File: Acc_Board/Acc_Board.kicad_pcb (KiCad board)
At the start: 2 copper layers, 165.1 x 69.8 mm, 58 parts, among them J1 1053091202, J11 1053091202, J12 776087-1, J2 1053091202, J3 1053091202, J4 1053091202, J5 1053091202, J6 1053091202, J7 IsoSPI, J9 1053091202, K1 Relay_SPST-NO, K2 Latching Relay, U1 ISO1050DUB, U10 DK1A1B-12V, U11 LM555N, U12 LTC6820, U13 R-78B5.0-2.0, U2 NUCLEO-L432KC, U4 PQDE6W-Q110-S5-H-D, U5 NAND, U6 NSL-32, U7 DK1A1B-12V, U8 NSL-32, U9 NSL-32

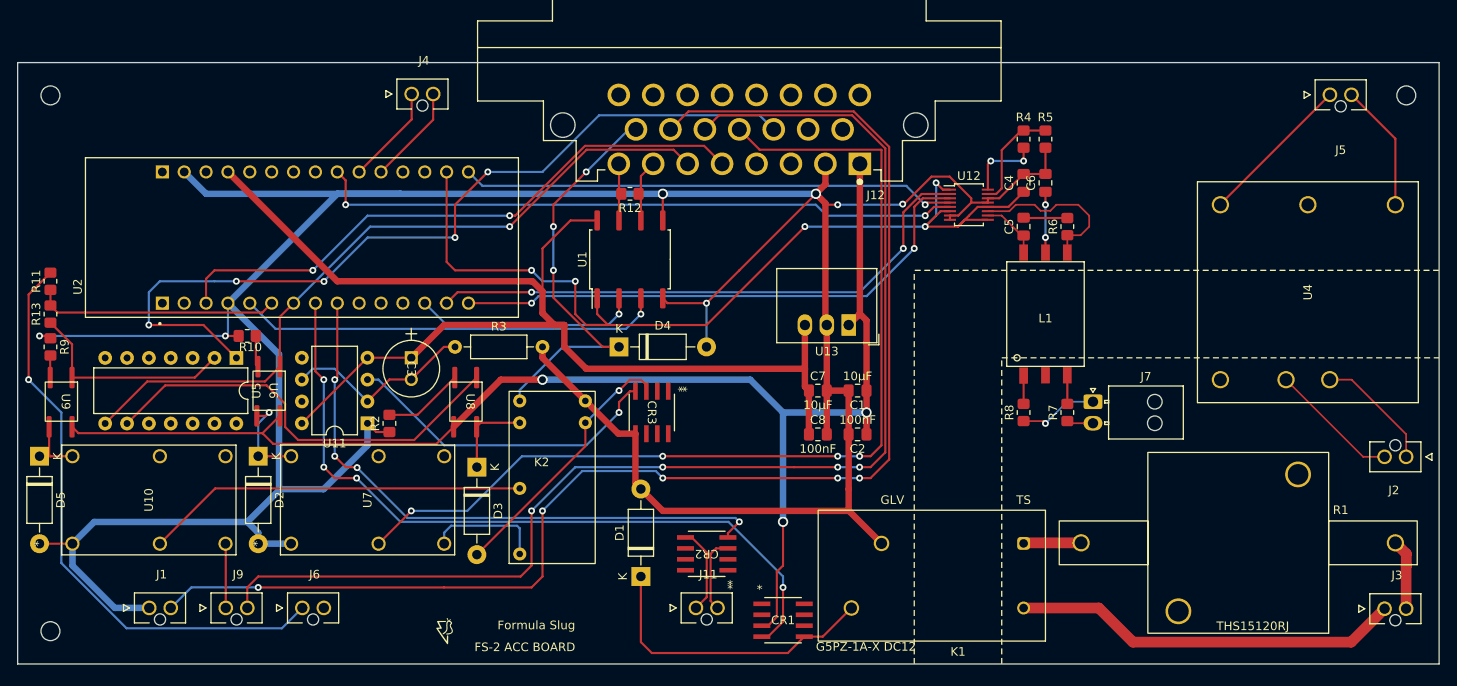
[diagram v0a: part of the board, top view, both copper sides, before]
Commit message: added 3d model for precharge resistor for acc board
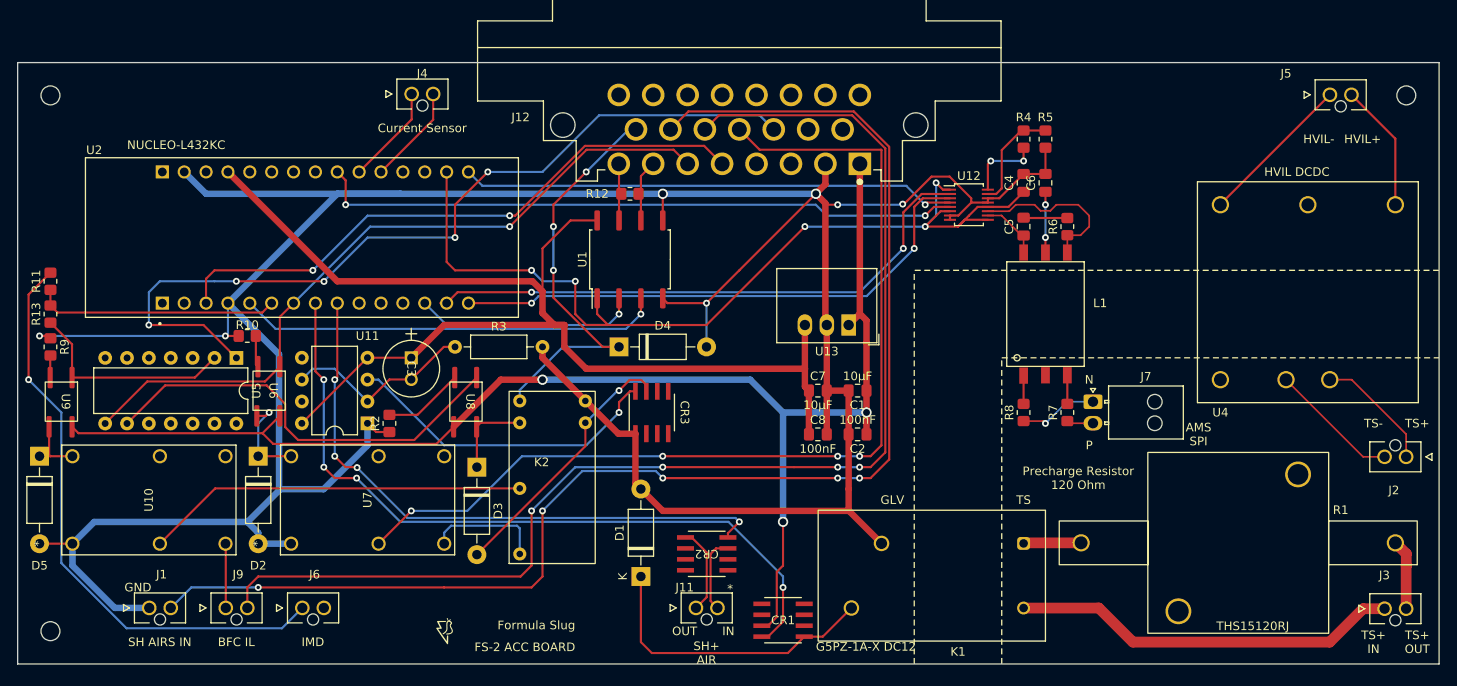
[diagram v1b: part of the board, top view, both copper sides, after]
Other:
- board text added: "AMS SPI"
- board text added: "BFC IL"
- board text added: "Current Sensor"
- board text added: "GND"
- board text added: "HVIL DCDC"
- board text added: "HVIL+"
- board text added: "HVIL-"
- board text added: "IMD"
- board text added: "IN"
- board text added: "N"
- board text added: "NUCLEO-L432KC"
- board text added: "OUT"
- board text added: "P"
- board text added: "Precharge Resistor 120 Ohm"
- board text added: "SH AIRS IN"
- board text added: "SH+ AIR"
- board text added: "TS+"
- board text added: "TS+ IN"
- board text added: "TS+ OUT"
- board text added: "TS-"

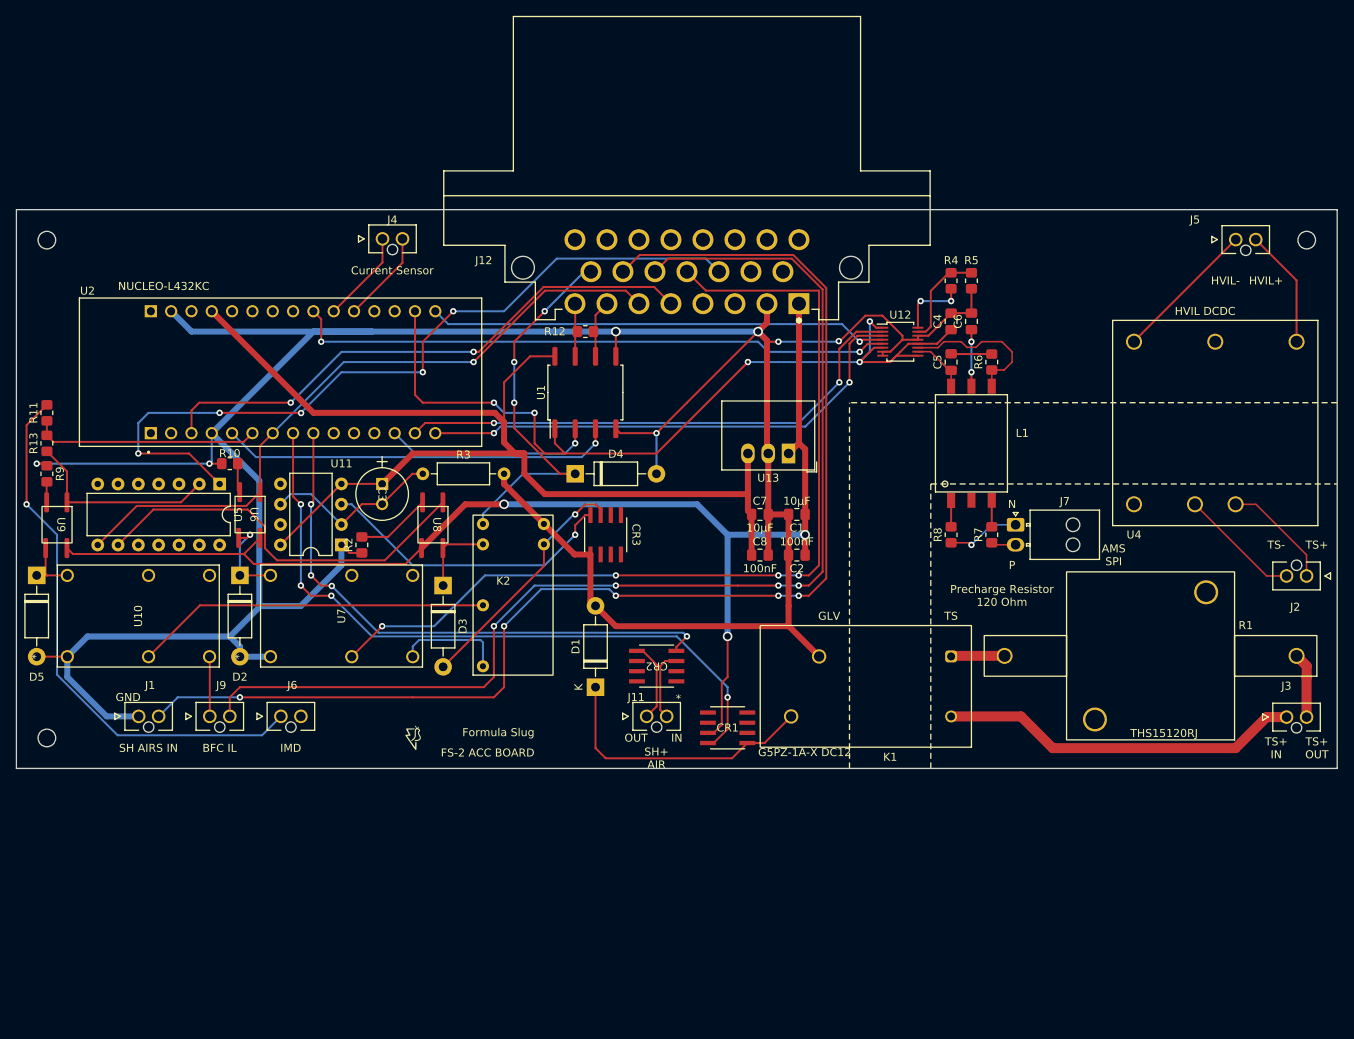
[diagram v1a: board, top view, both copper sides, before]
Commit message: Fixed op amps for current sensor on acc board
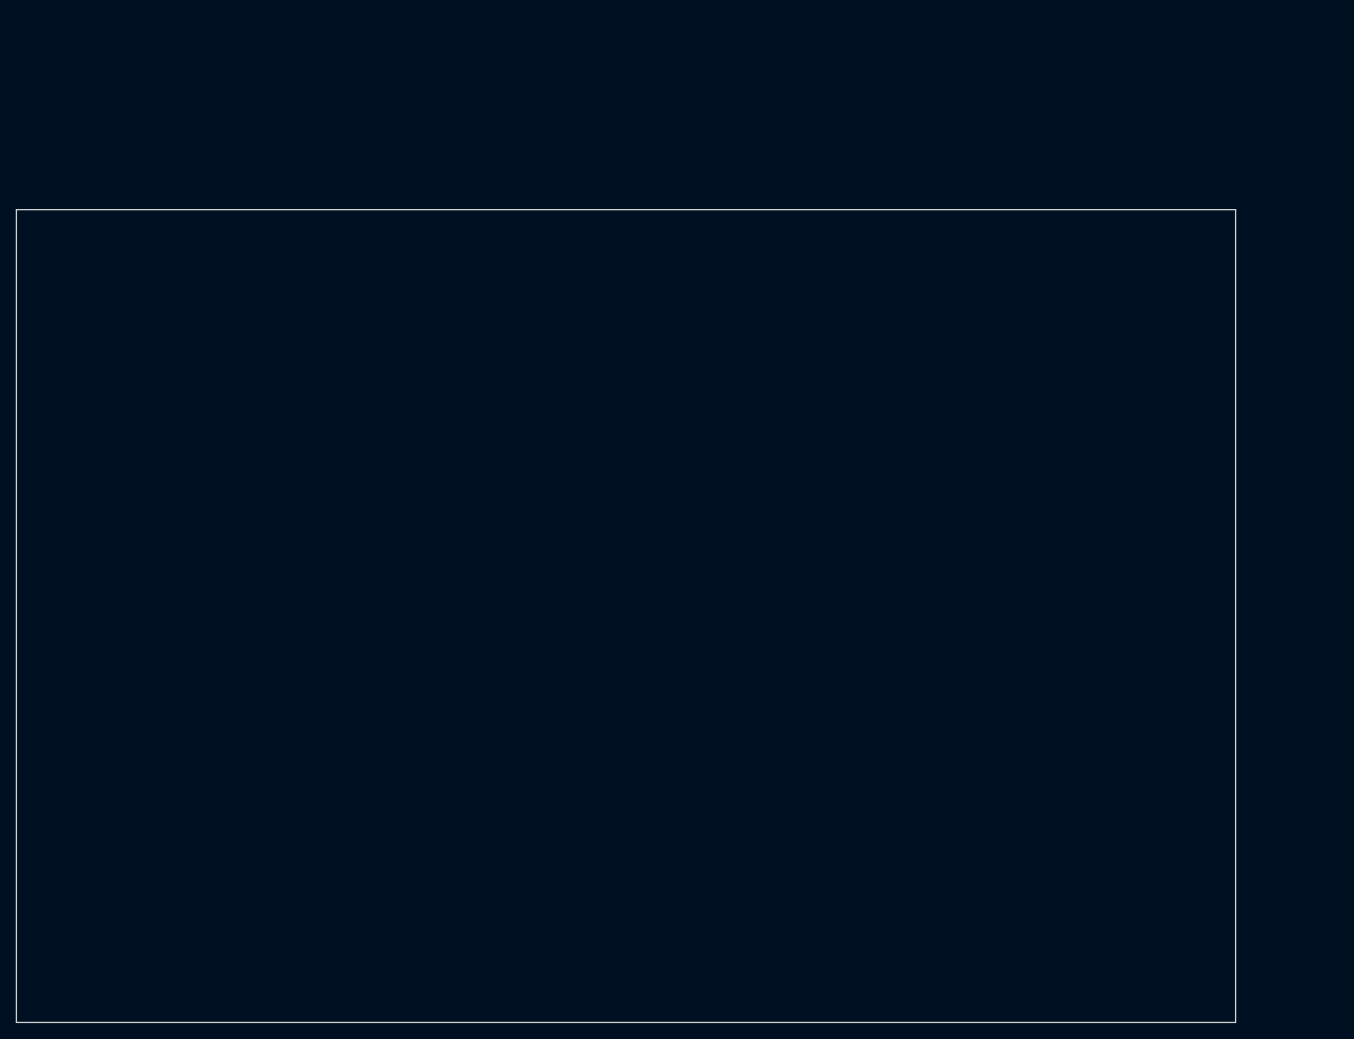
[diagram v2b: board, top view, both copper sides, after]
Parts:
- removed C1, C7: 10µF, Capacitor_SMD:C_0805_2012Metric_Pad1.18x1.45mm_HandSolder
- removed C2, C8: 100nF, Capacitor_SMD:C_0805_2012Metric_Pad1.18x1.45mm_HandSolder
- removed C3: ECA-2DHG010 1uF, 1FS_2_Global_Footprint_Library:PCAP_63x112_PAN
- removed C4, C6: 10nF, Capacitor_SMD:C_0805_2012Metric_Pad1.18x1.45mm_HandSolder
- removed C5: 15pF, Capacitor_SMD:C_0805_2012Metric_Pad1.18x1.45mm_HandSolder
- removed CR1, CR2, CR3: STS6NF20V, 1FS_2_Global_Footprint_Library:SO-8_STM
- removed D1: 1N4001, Diode_THT:D_DO-41_SOD81_P10.16mm_Horizontal
- removed D2, D3, D4, D5: D, Diode_THT:D_DO-41_SOD81_P10.16mm_Horizontal
- removed G***: LOGO, 1FS_2_Global_Footprint_Library:FORMULA SLUG
- removed J1, J11, J2, J3, J4, J5, J6, J9: 1053091202, 1FS_2_Global_Footprint_Library:MOLEX_1053091202
- removed J12: 776087-1, 1FS_2_Global_Footprint_Library:TE_776087-1
- removed J7: IsoSPI, Connector_Molex:Molex_Nano-Fit_105313-xx02_1x02_P2.50mm_Horizontal
- removed K1: Relay_SPST-NO, 1FS_2_Global_Footprint_Library:G5PZ-1A-X DC12
- removed K2: Latching Relay, 1FS_2_Global_Footprint_Library:Omron G6BK-1114P-US
- removed L1: HM2113ZNL, 1FS_2_Global_Footprint_Library:HM2113ZNL
- removed R1: 120, 1FS_2_Global_Footprint_Library:THS15120RJ
- removed R10, R2, R9: 480, Resistor_SMD:R_0805_2012Metric_Pad1.20x1.40mm_HandSolder
- removed R11: 1.6K, Resistor_SMD:R_0805_2012Metric_Pad1.20x1.40mm_HandSolder
- removed R12: 120, Resistor_SMD:R_0805_2012Metric_Pad1.20x1.40mm_HandSolder
- removed R13: 470, Resistor_SMD:R_0805_2012Metric_Pad1.20x1.40mm_HandSolder
- removed R3: 2.4M, Resistor_THT:R_Axial_DIN0207_L6.3mm_D2.5mm_P10.16mm_Horizontal
- removed R4: 1.5k, Resistor_SMD:R_0805_2012Metric_Pad1.20x1.40mm_HandSolder
- removed R5: 680, Resistor_SMD:R_0805_2012Metric_Pad1.20x1.40mm_HandSolder
- removed R6: 402, Resistor_SMD:R_0805_2012Metric_Pad1.20x1.40mm_HandSolder
- removed R7, R8: 22, Resistor_SMD:R_0805_2012Metric_Pad1.20x1.40mm_HandSolder
- removed REF** (x3): MountingHole_2.2mm_M2, MountingHole:MountingHole_2.2mm_M2
- removed U1: ISO1050DUB, Package_SO:SOP-8_6.62x9.15mm_P2.54mm
- removed U10, U7: DK1A1B-12V, 1FS_2_Global_Footprint_Library:RELAY_DK2A_PAN
- removed U11: LM555N, Package_DIP:DIP-8_W7.62mm
- removed U12: LTC6820, 1FS_2_Global_Footprint_Library:MSOP-16_[LTC6820]_10_thou_compat
- removed U13: R-78B5.0-2.0, Converter_DCDC:Converter_DCDC_RECOM_R-78B-2.0_THT
- removed U2: NUCLEO-L432KC, 1FS_2_Global_Footprint_Library:MODULE_NUCLEO-L432KC
- removed U4: PQDE6W-Q110-S5-H-D, 1FS_2_Global_Footprint_Library:PQDE6W-Q110-S5-H-D_CUI
- removed U5: NAND, Package_DIP:DIP-14_W7.62mm
- removed U6, U8, U9: NSL-32, 1FS_2_Global_Footprint_Library:OptoCoupler 6-SOP
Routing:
- net GND: track 391.2 -> 0.00 mm, vias 7 -> 0
- net +12V: track 160.4 -> 0.00 mm, vias 3 -> 0
- net /Shutdown_AIRS_IN: track 160.0 -> 0.00 mm, vias 5 -> 0
- net /Shutdown_ACC_OUT: track 145.2 -> 0.00 mm, vias 4 -> 0
- net +5V: track 142.0 -> 0.00 mm
- net /Shutdown_ACC_IN: track 114.9 -> 0.00 mm, vias 4 -> 0
- net +3.3V: track 107.7 -> 0.00 mm, vias 5 -> 0
- net /BSPD_FAULT: track 99.6 -> 0.00 mm, vias 5 -> 0
- net /Precharge_Relay: track 86.5 -> 0.00 mm, vias 4 -> 0
- net /BMS_FAULT: track 84.9 -> 0.00 mm, vias 1 -> 0
- net /Iso SPI/STM_NSS: track 75.4 -> 0.00 mm, vias 2 -> 0
- net /Precharge_Control: track 70.4 -> 0.00 mm, vias 4 -> 0
- net /IMD_Light: track 70.0 -> 0.00 mm, vias 2 -> 0
- net Net-(J6-Pad1): track 68.5 -> 0.00 mm, vias 1 -> 0
- net /Iso SPI/STM_MOSI: track 66.9 -> 0.00 mm, vias 2 -> 0
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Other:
- board size 165.1 x 69.8 mm -> 152.4 x 101.6 mm
- board text removed: "AMS SPI"
- board text removed: "BFC IL"
- board text removed: "Current Sensor"
- board text removed: "FS-2 ACC BOARD"
- board text removed: "Formula Slug"
- board text removed: "GLV"
- board text removed: "GND"
- board text removed: "HVIL DCDC"
- board text removed: "HVIL+"
- board text removed: "HVIL-"
- board text removed: "IMD"
- board text removed: "IN"
- board text removed: "N"
- board text removed: "NUCLEO-L432KC"
- board text removed: "OUT"
- board text removed: "P"
- board text removed: "Precharge Resistor 120 Ohm"
- board text removed: "SH AIRS IN"
- board text removed: "SH+ AIR"
- board text removed: "TS"
- board text removed: "TS+"
- board text removed: "TS+ IN"
- board text removed: "TS+ OUT"
- board text removed: "TS-"
